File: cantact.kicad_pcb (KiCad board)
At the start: 2 copper layers, 36.1 x 59.9 mm, 51 parts, among them J1 Cantact, P2 SWD, P4 USB_C_Plug_USB2.0, U1 STM32F042C6T6, U3 MCP2551-I/SN, U4 XC6220B331MR-G, Y1 16 Mhz

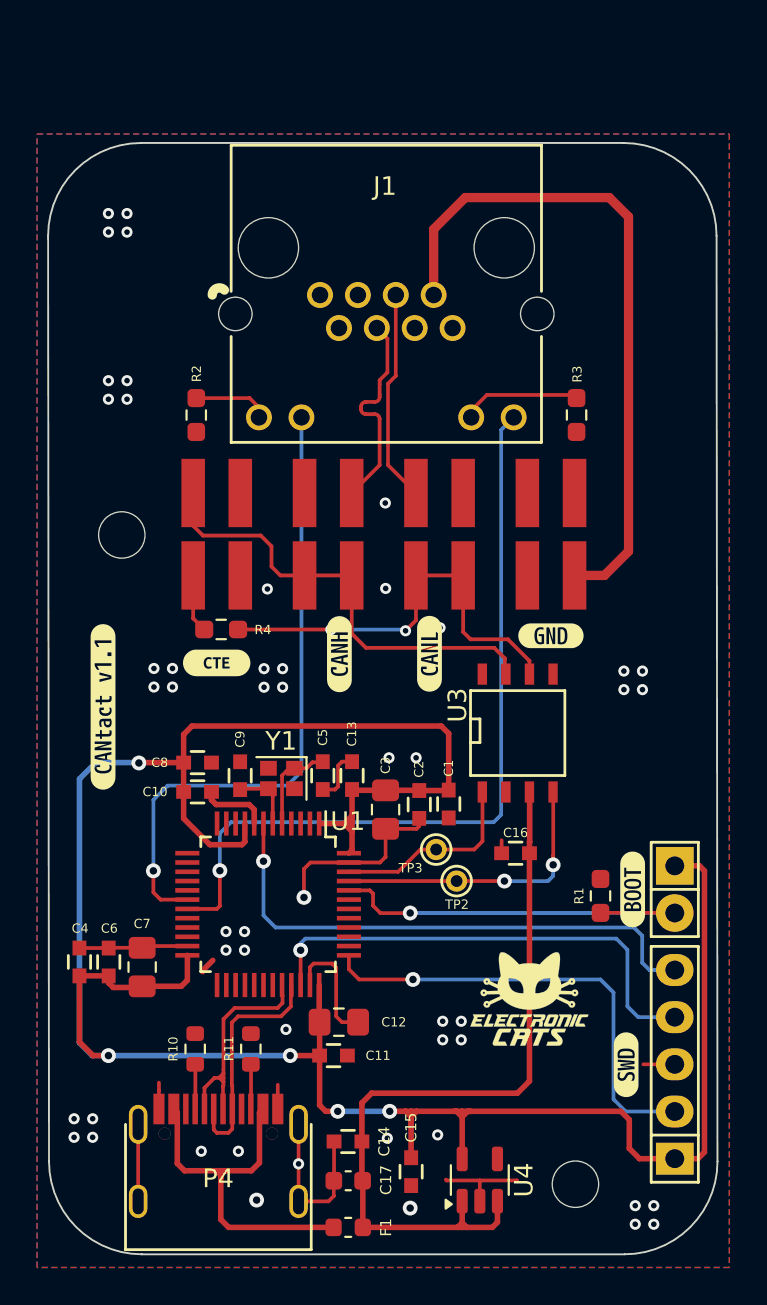
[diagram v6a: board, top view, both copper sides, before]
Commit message: Fix: CANbus routing and added 3D models
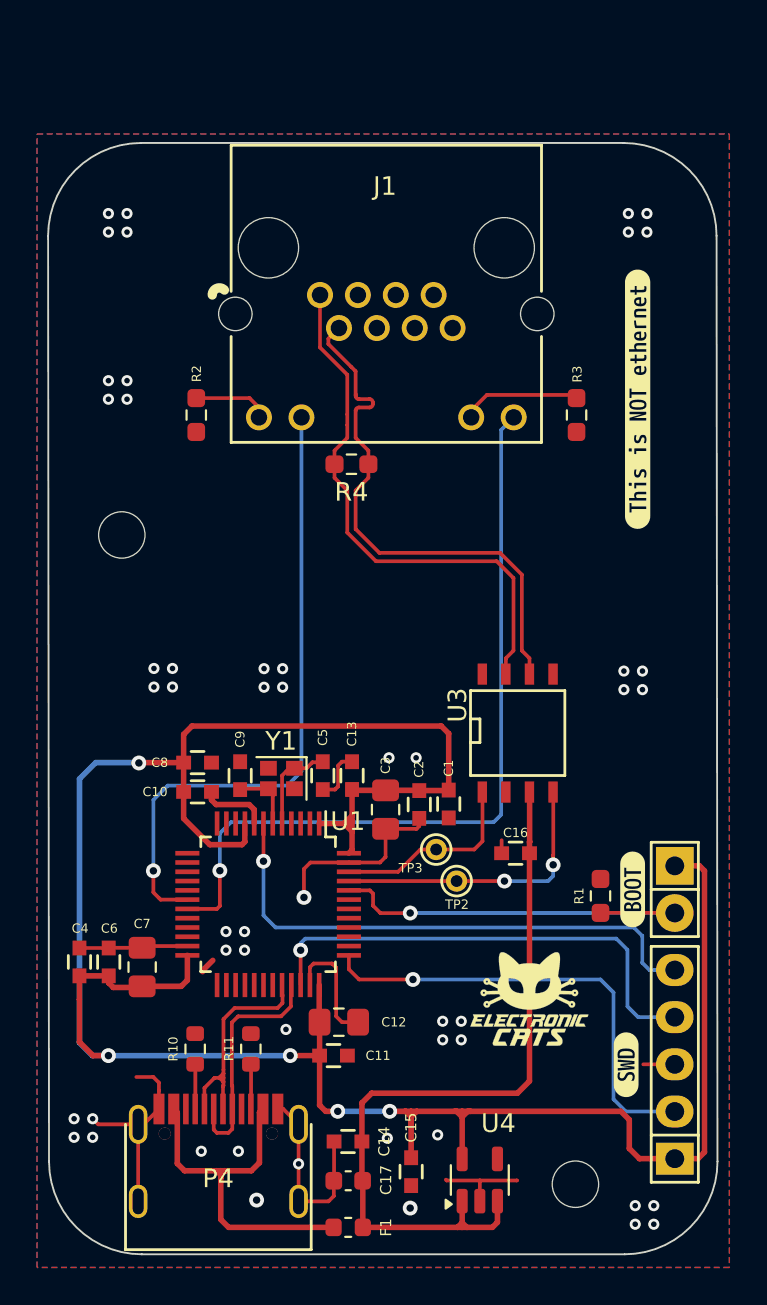
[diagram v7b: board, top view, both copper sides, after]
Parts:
- removed JP2: Term Enable, cantact:0015912040
- removed JP3: CANH Select, cantact:0015912040
- removed JP4: CANL Select, cantact:0015912040
- removed JP5: GND Select, cantact:0015912040
- removed kibuzzard-67FD8EE3: G***, kibuzzard-67FD8EE3
- removed kibuzzard-67FE7B2A: G***, kibuzzard-67FE7B2A
- removed kibuzzard-67FE7B45: G***, kibuzzard-67FE7B45
- removed the kibuzzard-67FE8A9D at (127.2, 122.6)
- removed kibuzzard-67FEBEE5: G***, kibuzzard-67FEBEE5
- added kibuzzard-6802DBB7: G***, kibuzzard-6802DBB7, F.Cu at (156.0, 106.0)
- moved R4 11.3 mm to (140.6, 109.5)
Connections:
- J1 pad 1: unconnected-(J1-Pad1) -> /CAN+
- J1 pad 2: unconnected-(J1-Pad2) -> /CAN-
- J1 pad 3: unconnected-(J1-Pad3) -> GND
- J1 pad 4: /CAN+ -> unconnected-(J1-Pad4)
- J1 pad 5: /CAN- -> unconnected-(J1-Pad5)
- J1 pad 7: /GND1 -> unconnected-(J1-Pad7)
- R4 pad 1: Net-(JP4-Pin_1) -> /CAN-
- R4 pad 2: Net-(JP2-Pin_1) -> /CAN+
- U3 pad 6: Net-(JP4-Pin_1) -> /CAN-
- U3 pad 7: Net-(JP2-Pin_2) -> /CAN+
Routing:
- net /GND1: track 36.4 -> 0.00 mm
- net Net-(JP2-Pin_2): track 24.9 -> 0.00 mm
- net Net-(JP4-Pin_1): track 22.8 -> 0.00 mm, vias 2 -> 0
- net /CAN+: track 11.5 -> 29.4 mm
- net /CAN-: track 11.8 -> 29.3 mm
- net GND: track 53.4 -> 58.9 mm
- net Net-(JP2-Pin_1): track 3.16 -> 0.00 mm

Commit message: fix(hw): update labels
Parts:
- added kibuzzard-67FE8A9D: G***, kibuzzard-67FE8A9D, F.Cu at (141.5, 117.5)
- moved kibuzzard-6802DBB7 5.70 mm to (154.5, 100.5)
